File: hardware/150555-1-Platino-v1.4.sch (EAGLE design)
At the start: 88 parts, among them IC1 MEGA164P/324P/644P-PU, IC2 MEGA48/88/168-PU, IC3 7805TV, IC4 MCP1700-3302, K1 EXT1, K10 K-HEADER-MALE-1X5-V, K11 K-HEADER-MALE-1X5-V, K12 K-TERMINAL-BLOCK-1X2-350, K2 K-HEADER-MALE-1X6-H, K3 K-HEADER-MALE-2X3-V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

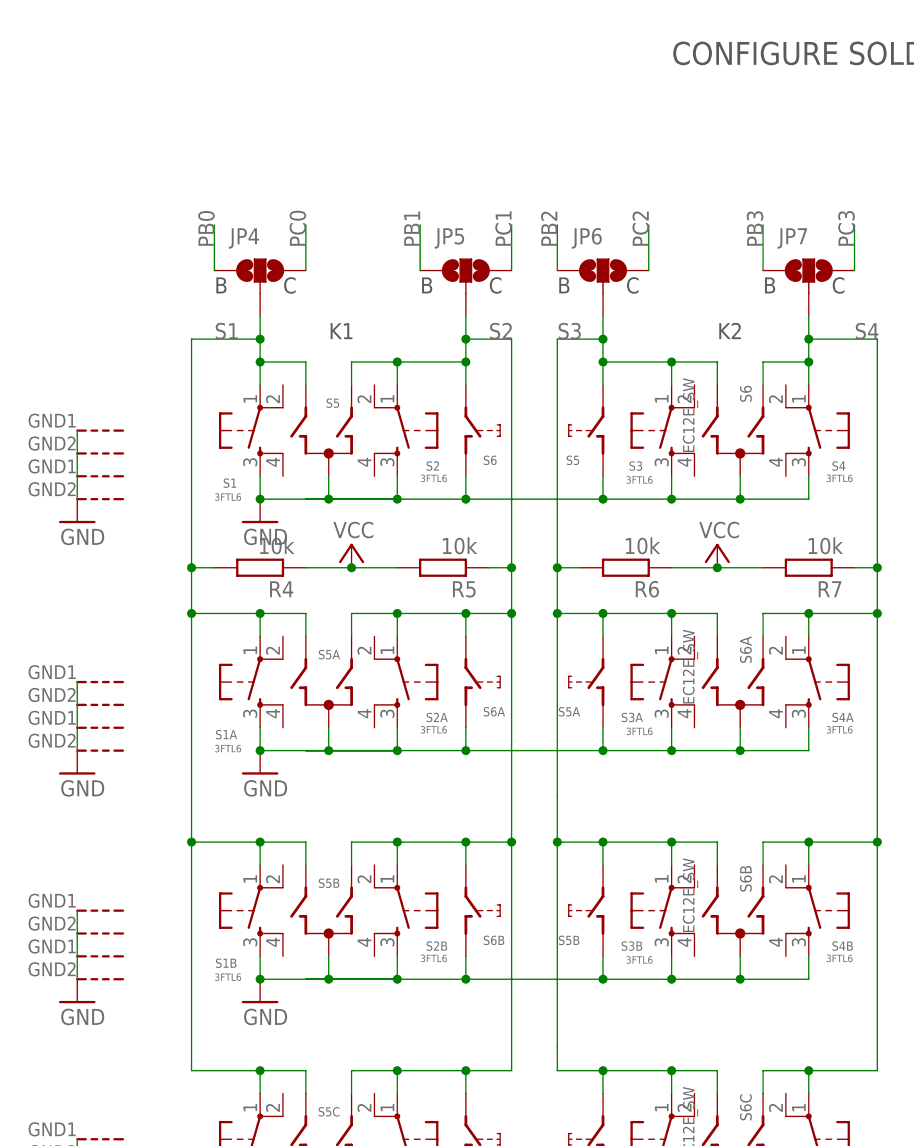
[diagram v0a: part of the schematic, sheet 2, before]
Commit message: Release
Fixed all OAR and hole-in-hole issues.
Minor silkscreen edits.
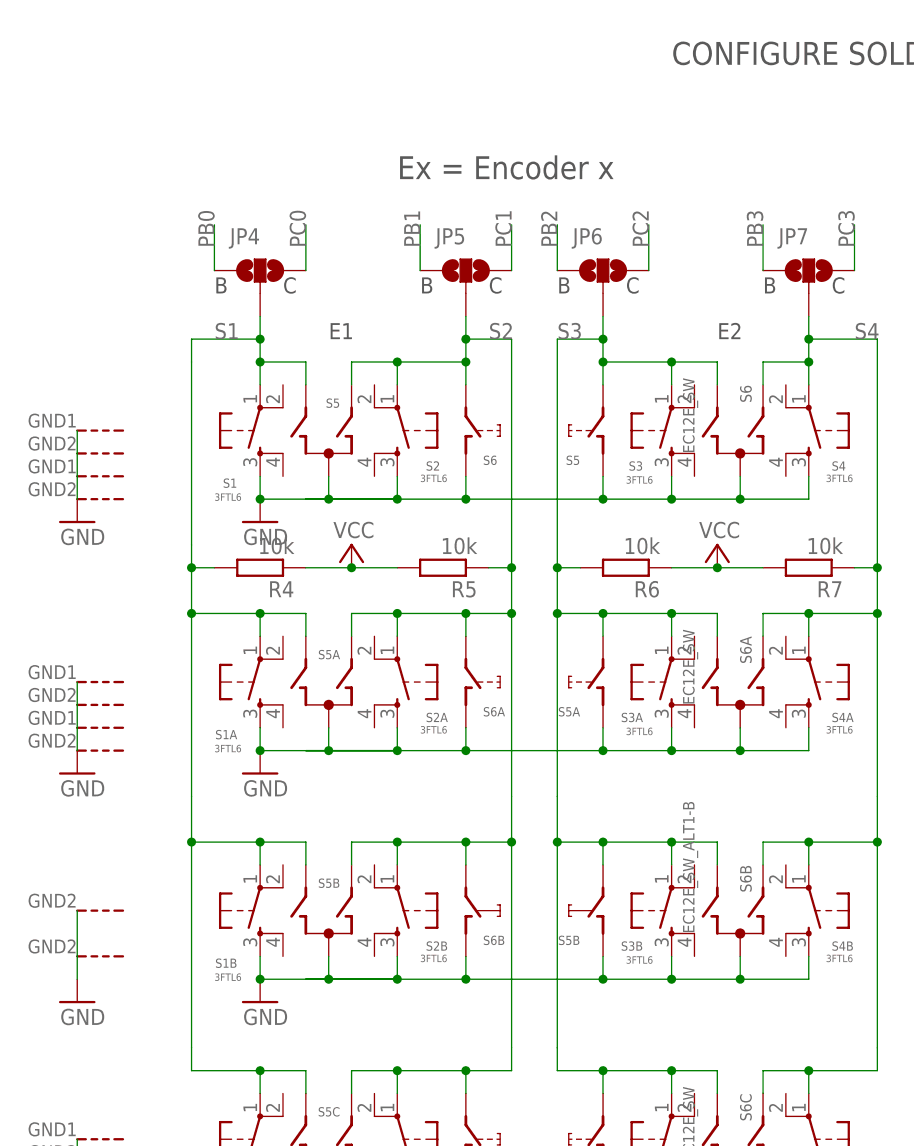
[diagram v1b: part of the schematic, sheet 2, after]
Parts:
- S5B, S6B: value EC12E_SW -> EC12E_SW_ALT1-B; device 000_cpv:EC12E_SW -> 150555-1-Platino-v1.4:EC12E_SW_ALT1-B
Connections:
- net GND: no longer S5BG$4.G, S6BG$4.G
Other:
- note added: "E1"
- note added: "E2"
- note added: "Ex = Encoder x"
- note removed: "K1"
- note removed: "K2"
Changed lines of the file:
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@@
 <?xml version="1.0" encoding="utf-8"?>
 <!DOCTYPE eagle SYSTEM "eagle.dtd">
-<eagle version="6.5.0">
+<eagle version="7.3.0">
 <drawing>
 <settings>
@@
 <part name="S6C" library="000_cpv" deviceset="EC12E_SW" device=""/>
 <part name="GND20" library="supply1" deviceset="GND" device=""/>
-<part name="S5B" library="000_cpv" deviceset="EC12E_SW" device=""/>
+<part name="S5B" library="150555-1-Platino-v1.4" deviceset="EC12E_SW_ALT1" device="-B"/>
 <part name="S2B" library="000_cpv" deviceset="PUSHBUTTON_MULTIMEC" device="" value="3FTL6"/>
 <part name="S1B" library="000_cpv" deviceset="PUSHBUTTON_MULTIMEC" device="" value="3FTL6"/>
 <part name="S4B" library="000_cpv" deviceset="PUSHBUTTON_MULTIMEC" device="" value="3FTL6"/>
 <part name="S3B" library="000_cpv" deviceset="PUSHBUTTON_MULTIMEC" device="" value="3FTL6"/>
-<part name="S6B" library="000_cpv" deviceset="EC12E_SW" device=""/>
+<part name="S6B" library="150555-1-Platino-v1.4" deviceset="EC12E_SW_ALT1" device="-B"/>
 <part name="GND21" library="supply1" deviceset="GND" device=""/>
 <part name="K10" library="elpp-tht-v1.3" deviceset="K-HEADER-MALE-1X5-" device="V"/>
@@
 <text x="99.06" y="157.48" size="2.54" layer="97">CONFIGURE SOLDER JUMPERS FIRST</text>
 <text x="121.92" y="12.7" size="6.4516" layer="97">PLATINO</text>
-<text x="60.96" y="127" size="1.778" layer="97">K1</text>
-<text x="104.14" y="127" size="1.778" layer="97">K2</text>
+<text x="60.96" y="127" size="1.778" layer="97">E1</text>
+<text x="104.14" y="127" size="1.778" layer="97">E2</text>
 <text x="226.06" y="109.22" size="1.778" layer="97">B</text>
 <text x="226.06" y="93.98" size="1.778" layer="97">B</text>
@@
 <text x="218.44" y="142.24" size="1.778" layer="97">D</text>
 <text x="218.44" y="160.02" size="1.778" layer="97">D</text>
+<text x="68.58" y="144.78" size="2.54" layer="97">Ex = Encoder x</text>
 </plain>
 <instances>
@@
 </instance>
 <instance part="S5B" gate="G$3" x="33.02" y="63.5"/>
-<instance part="S5B" gate="G$4" x="33.02" y="60.96"/>
 <instance part="S2B" gate="G$1" x="68.58" y="63.5" smashed="yes" rot="R270">
 <attribute name="NAME" x="71.755" y="59.055" size="1.016" layer="95"/>
@@
 </instance>
 <instance part="S6B" gate="G$3" x="33.02" y="58.42"/>
-<instance part="S6B" gate="G$4" x="33.02" y="55.88"/>
 <instance part="GND21" gate="1" x="53.34" y="53.34" smashed="yes">
 <attribute name="VALUE" x="51.435" y="50.8" size="1.778" layer="96"/>
@@
 <segment>
 <wire x1="33.02" y1="55.88" x2="33.02" y2="58.42" width="0.1524" layer="91"/>
-<wire x1="33.02" y1="58.42" x2="33.02" y2="60.96" width="0.1524" layer="91"/>
-<wire x1="33.02" y1="60.96" x2="33.02" y2="63.5" width="0.1524" layer="91"/>
-<pinref part="S6B" gate="G$4" pin="G"/>
+<wire x1="33.02" y1="58.42" x2="33.02" y2="63.5" width="0.1524" layer="91"/>
 <pinref part="GND23" gate="1" pin="GND"/>
 <pinref part="S6B" gate="G$3" pin="G"/>
-<pinref part="S5B" gate="G$4" pin="G"/>
 <pinref part="S5B" gate="G$3" pin="G"/>
 </segment>
